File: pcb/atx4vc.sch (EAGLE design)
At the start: 76 parts, among them IC2 REG1117, IC3 STM32F042F4, IC4 MY_7905DT, J1 ATX24RH, SW1 324_SW, SW2 324_SW, SW3 324_SW, SW4 324_SW, SW5 324_SW, SW7 324_SW, U1 USBC_16P, U2 USBC_16P

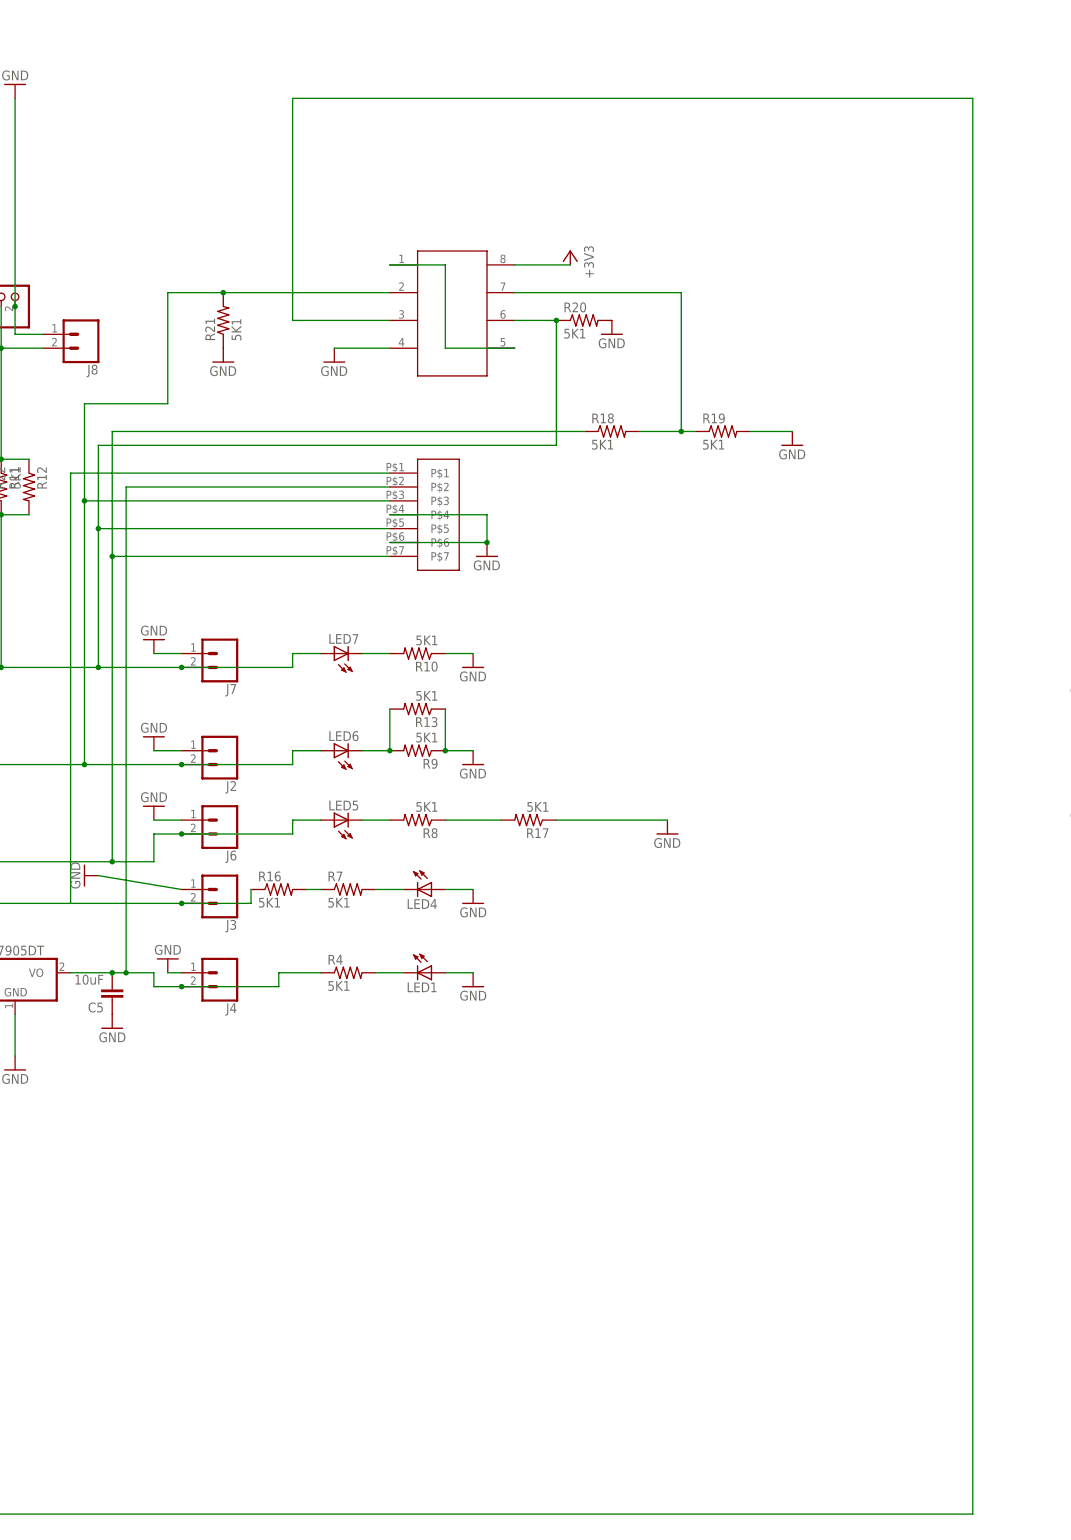
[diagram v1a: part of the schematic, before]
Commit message: updated fuse detect chip trace
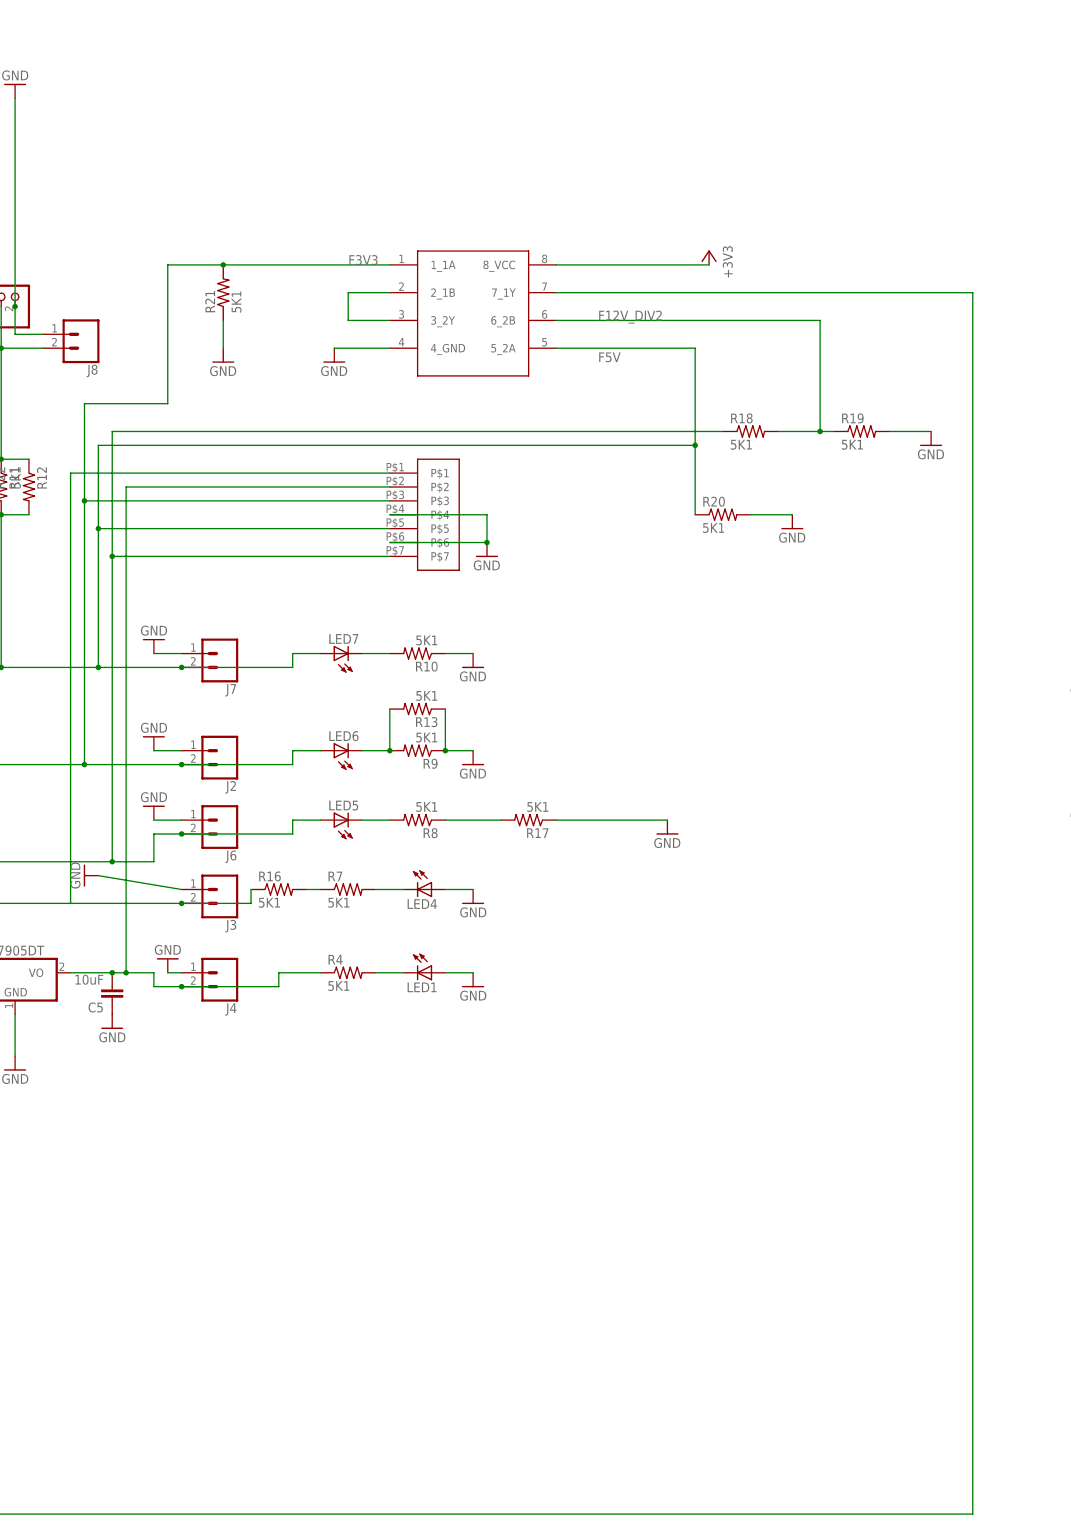
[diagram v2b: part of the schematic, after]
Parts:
- U$6: value 74LVC2G08SSOP8 -> 74LVC2G08; device atx4vc:74LVC2G08SSOP8 -> atx4vc:74LVC2G08
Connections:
- net N$15 renamed F12V
- removed net N$16: J2.2, LED6.A, R21.2, U$4.P$3, U$6.2_1B, U$7.B0, U$7.B1
- removed net N$30: J7.2, JP12.1, JP7.1, LED7.A, R11.2, R12.2, R20.1, R22.2, U$4.P$5, U$6.6_2B, U$8.B0, U$8.B1, U1.VBUS
- removed net N$39: R18.2, R19.1, U$6.7_1Y
- new net F12V_DIV2: R18.2, R19.1, U$6.6_2B
- new net F3V3: J2.2, LED6.A, R21.2, U$4.P$3, U$6.1_1A, U$7.B0, U$7.B1
- new net F5V: J7.2, JP12.1, JP7.1, LED7.A, R11.2, R12.2, R20.1, R22.2, U$4.P$5, U$6.5_2A, U$8.B0, U$8.B1, U1.VBUS
- net N$12: now also U$6.2_1B, U$6.3_2Y; no longer U$6.1_1A, U$6.5_2A
- net N$24: now also U$6.7_1Y; no longer U$6.3_2Y
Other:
- moved on the sheet: R18, R19, R20, R21
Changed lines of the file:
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@@
 <part name="JP13" library="SparkFun-Jumpers" deviceset="JUMPER-SMT_2_NO" device="_NO-SILK"/>
 <part name="JP14" library="SparkFun-Jumpers" deviceset="JUMPER-SMT_2_NO" device="_NO-SILK"/>
-<part name="U$6" library="atx4vc" deviceset="74LVC2G08" device="SSOP8"/>
+<part name="U$6" library="atx4vc" deviceset="74LVC2G08" device="" value="74LVC2G08"/>
 <part name="U$4" library="396_conn" deviceset="VH396" device=""/>
 <part name="JP10" library="adafruit" deviceset="PINHD-1X1" device="CB"/>
@@
 <attribute name="VALUE" x="401.32" y="58.42" size="1.778" layer="96"/>
 </instance>
-<instance part="+3V4" gate="G$1" x="419.1" y="116.84" smashed="yes" rot="MR0">
-<attribute name="VALUE" x="421.64" y="111.76" size="1.778" layer="96" rot="MR90"/>
+<instance part="+3V4" gate="G$1" x="444.5" y="116.84" smashed="yes" rot="MR0">
+<attribute name="VALUE" x="447.04" y="111.76" size="1.778" layer="96" rot="MR90"/>
 </instance>
 <instance part="GND38" gate="1" x="375.92" y="96.52" smashed="yes">
@@
 <attribute name="VALUE" x="-34.29" y="-119.38" size="1.778" layer="96"/>
 </instance>
-<instance part="R18" gate="G$1" x="426.72" y="83.82" smashed="yes">
-<attribute name="NAME" x="422.91" y="85.3186" size="1.778" layer="95"/>
-<attribute name="VALUE" x="422.91" y="80.518" size="1.778" layer="96"/>
-</instance>
-<instance part="R19" gate="G$1" x="447.04" y="83.82" smashed="yes">
-<attribute name="NAME" x="443.23" y="85.3186" size="1.778" layer="95"/>
-<attribute name="VALUE" x="443.23" y="80.518" size="1.778" layer="96"/>
-</instance>
-<instance part="GND39" gate="1" x="459.74" y="81.28" smashed="yes">
-<attribute name="VALUE" x="457.2" y="78.74" size="1.778" layer="96"/>
-</instance>
-<instance part="R20" gate="G$1" x="421.64" y="104.14" smashed="yes">
-<attribute name="NAME" x="417.83" y="105.6386" size="1.778" layer="95"/>
-<attribute name="VALUE" x="417.83" y="100.838" size="1.778" layer="96"/>
-</instance>
-<instance part="GND40" gate="1" x="426.72" y="101.6" smashed="yes">
-<attribute name="VALUE" x="424.18" y="99.06" size="1.778" layer="96"/>
-</instance>
-<instance part="R21" gate="G$1" x="355.6" y="104.14" smashed="yes" rot="R90">
-<attribute name="NAME" x="354.1014" y="100.33" size="1.778" layer="95" rot="R90"/>
-<attribute name="VALUE" x="358.902" y="100.33" size="1.778" layer="96" rot="R90"/>
+<instance part="R18" gate="G$1" x="452.12" y="83.82" smashed="yes">
+<attribute name="NAME" x="448.31" y="85.3186" size="1.778" layer="95"/>
+<attribute name="VALUE" x="448.31" y="80.518" size="1.778" layer="96"/>
+</instance>
+<instance part="R19" gate="G$1" x="472.44" y="83.82" smashed="yes">
+<attribute name="NAME" x="468.63" y="85.3186" size="1.778" layer="95"/>
+<attribute name="VALUE" x="468.63" y="80.518" size="1.778" layer="96"/>
+</instance>
+<instance part="GND39" gate="1" x="485.14" y="81.28" smashed="yes">
+<attribute name="VALUE" x="482.6" y="78.74" size="1.778" layer="96"/>
+</instance>
+<instance part="R20" gate="G$1" x="447.04" y="68.58" smashed="yes">
+<attribute name="NAME" x="443.23" y="70.0786" size="1.778" layer="95"/>
+<attribute name="VALUE" x="443.23" y="65.278" size="1.778" layer="96"/>
+</instance>
+<instance part="GND40" gate="1" x="459.74" y="66.04" smashed="yes">
+<attribute name="VALUE" x="457.2" y="63.5" size="1.778" layer="96"/>
+</instance>
+<instance part="R21" gate="G$1" x="355.6" y="109.22" smashed="yes" rot="R90">
+<attribute name="NAME" x="354.1014" y="105.41" size="1.778" layer="95" rot="R90"/>
+<attribute name="VALUE" x="358.902" y="105.41" size="1.778" layer="96" rot="R90"/>
 </instance>
 <instance part="GND41" gate="1" x="355.6" y="96.52" smashed="yes">
@@
 <pinref part="R19" gate="G$1" pin="2"/>
 <pinref part="GND39" gate="1" pin="GND"/>
-<wire x1="452.12" y1="83.82" x2="459.74" y2="83.82" width="0.1524" layer="91"/>
+<wire x1="477.52" y1="83.82" x2="485.14" y2="83.82" width="0.1524" layer="91"/>
 </segment>
 <segment>
 <pinref part="R20" gate="G$1" pin="2"/>
 <pinref part="GND40" gate="1" pin="GND"/>
+<wire x1="452.12" y1="68.58" x2="459.74" y2="68.58" width="0.1524" layer="91"/>
 </segment>
 <segment>
 <pinref part="R21" gate="G$1" pin="1"/>
 <pinref part="GND41" gate="1" pin="GND"/>
+<wire x1="355.6" y1="104.14" x2="355.6" y2="99.06" width="0.1524" layer="91"/>
 </segment>
 </net>
@@
 <pinref part="+3V4" gate="G$1" pin="+3V3"/>
 <pinref part="U$6" gate="G$1" pin="8_VCC"/>
-<wire x1="419.1" y1="114.3" x2="408.94" y2="114.3" width="0.1524" layer="91"/>
+<wire x1="444.5" y1="114.3" x2="416.56" y2="114.3" width="0.1524" layer="91"/>
 </segment>
 </net>
@@
 </segment>
 </net>
-<net name="N$30" class="0">
+<net name="F5V" class="0">
 <segment>
 <pinref part="LED7" gate="G$1" pin="A"/>
@@
 <junction x="332.74" y="40.64"/>
 <wire x1="332.74" y1="66.04" x2="332.74" y2="81.28" width="0.1524" layer="91"/>
-<wire x1="332.74" y1="81.28" x2="416.56" y2="81.28" width="0.1524" layer="91"/>
+<wire x1="332.74" y1="81.28" x2="441.96" y2="81.28" width="0.1524" layer="91"/>
 <junction x="332.74" y="66.04"/>
-<pinref part="U$6" gate="G$1" pin="6_2B"/>
-<wire x1="408.94" y1="104.14" x2="416.56" y2="104.14" width="0.1524" layer="91"/>
-<wire x1="416.56" y1="104.14" x2="416.56" y2="81.28" width="0.1524" layer="91"/>
+<wire x1="441.96" y1="68.58" x2="441.96" y2="81.28" width="0.1524" layer="91"/>
 <pinref part="R20" gate="G$1" pin="1"/>
-<junction x="416.56" y="104.14"/>
 <pinref part="R22" gate="G$1" pin="2"/>
 <wire x1="314.96" y1="68.58" x2="312.42" y2="68.58" width="0.1524" layer="91"/>
-</segment>
-</net>
-<net name="N$15" class="0">
+<pinref part="U$6" gate="G$1" pin="5_2A"/>
+<wire x1="441.96" y1="81.28" x2="441.96" y2="99.06" width="0.1524" layer="91"/>
+<wire x1="441.96" y1="99.06" x2="416.56" y2="99.06" width="0.1524" layer="91"/>
+<junction x="441.96" y="81.28"/>
+<label x="424.18" y="96.52" size="1.778" layer="95"/>
+</segment>
+</net>
+<net name="F12V" class="0">
 <segment>
 <pinref part="LED5" gate="G$1" pin="A"/>
@@
 <junction x="335.28" y="5.08"/>
 <wire x1="335.28" y1="60.96" x2="335.28" y2="83.82" width="0.1524" layer="91"/>
-<wire x1="335.28" y1="83.82" x2="421.64" y2="83.82" width="0.1524" layer="91"/>
+<wire x1="335.28" y1="83.82" x2="447.04" y2="83.82" width="0.1524" layer="91"/>
 <junction x="335.28" y="60.96"/>
 <pinref part="R18" gate="G$1" pin="1"/>
 </segment>
 </net>
-<net name="N$16" class="0">
+<net name="F3V3" class="0">
 <segment>
 <pinref part="LED6" gate="G$1" pin="A"/>
@@
 <junction x="330.2" y="71.12"/>
 <wire x1="330.2" y1="88.9" x2="345.44" y2="88.9" width="0.1524" layer="91"/>
-<wire x1="345.44" y1="88.9" x2="345.44" y2="109.22" width="0.1524" layer="91"/>
-<wire x1="345.44" y1="109.22" x2="355.6" y2="109.22" width="0.1524" layer="91"/>
-<pinref part="U$6" gate="G$1" pin="2_1B"/>
+<wire x1="345.44" y1="88.9" x2="345.44" y2="114.3" width="0.1524" layer="91"/>
+<wire x1="345.44" y1="114.3" x2="355.6" y2="114.3" width="0.1524" layer="91"/>
 <pinref part="R21" gate="G$1" pin="2"/>
-<wire x1="355.6" y1="109.22" x2="386.08" y2="109.22" width="0.1524" layer="91"/>
-<junction x="355.6" y="109.22"/>
+<pinref part="U$6" gate="G$1" pin="1_1A"/>
+<wire x1="355.6" y1="114.3" x2="386.08" y2="114.3" width="0.1524" layer="91"/>
+<junction x="355.6" y="114.3"/>
+<label x="378.46" y="114.3" size="1.778" layer="95"/>
 </segment>
 </net>
@@
 </segment>
 </net>
-<net name="N$12" class="0">
-<segment>
-<pinref part="U$6" gate="G$1" pin="5_2A"/>
-<wire x1="408.94" y1="99.06" x2="396.24" y2="99.06" width="0.1524" layer="91"/>
-<wire x1="396.24" y1="99.06" x2="396.24" y2="114.3" width="0.1524" layer="91"/>
-<pinref part="U$6" gate="G$1" pin="1_1A"/>
-<wire x1="396.24" y1="114.3" x2="386.08" y2="114.3" width="0.1524" layer="91"/>
-</segment>
-</net>
 <net name="N$24" class="0">
 <segment>
-<pinref part="U$6" gate="G$1" pin="3_2Y"/>
-<wire x1="386.08" y1="104.14" x2="368.3" y2="104.14" width="0.1524" layer="91"/>
-<wire x1="368.3" y1="104.14" x2="368.3" y2="144.78" width="0.1524" layer="91"/>
-<wire x1="368.3" y1="144.78" x2="492.76" y2="144.78" width="0.1524" layer="91"/>
-<wire x1="492.76" y1="144.78" x2="492.76" y2="-114.3" width="0.1524" layer="91"/>
+<wire x1="492.76" y1="109.22" x2="492.76" y2="-114.3" width="0.1524" layer="91"/>
 <wire x1="492.76" y1="-114.3" x2="-30.48" y2="-114.3" width="0.1524" layer="91"/>
 <pinref part="JP3" gate="G$1" pin="2"/>
+<pinref part="U$6" gate="G$1" pin="7_1Y"/>
+<wire x1="416.56" y1="109.22" x2="492.76" y2="109.22" width="0.1524" layer="91"/>
 </segment>
 </net>
@@
 </segment>
 </net>
-<net name="N$39" class="0">
+<net name="F12V_DIV2" class="0">
 <segment>
 <pinref part="R18" gate="G$1" pin="2"/>
 <pinref part="R19" gate="G$1" pin="1"/>
-<wire x1="441.96" y1="83.82" x2="439.42" y2="83.82" width="0.1524" layer="91"/>
-<pinref part="U$6" gate="G$1" pin="7_1Y"/>
-<wire x1="439.42" y1="83.82" x2="431.8" y2="83.82" width="0.1524" layer="91"/>
-<wire x1="439.42" y1="83.82" x2="439.42" y2="109.22" width="0.1524" layer="91"/>
-<wire x1="439.42" y1="109.22" x2="408.94" y2="109.22" width="0.1524" layer="91"/>
-<junction x="439.42" y="83.82"/>
-</segment>
-</net>
+<wire x1="467.36" y1="83.82" x2="464.82" y2="83.82" width="0.1524" layer="91"/>
+<wire x1="464.82" y1="83.82" x2="457.2" y2="83.82" width="0.1524" layer="91"/>
+<wire x1="464.82" y1="83.82" x2="464.82" y2="104.14" width="0.1524" layer="91"/>
+<junction x="464.82" y="83.82"/>
+<pinref part="U$6" gate="G$1" pin="6_2B"/>
+<wire x1="416.56" y1="104.14" x2="464.82" y2="104.14" width="0.1524" layer="91"/>
+<label x="424.18" y="104.14" size="1.778" layer="95"/>
+</segment>
+</net>
+<net name="N$12" class="0">
+<segment>
+<pinref part="U$6" gate="G$1" pin="3_2Y"/>
+<wire x1="386.08" y1="104.14" x2="378.46" y2="104.14" width="0.1524" layer="91"/>
+<wire x1="378.46" y1="104.14" x2="378.46" y2="109.22" width="0.1524" layer="91"/>
+<pinref part="U$6" gate="G$1" pin="2_1B"/>
+<wire x1="378.46" y1="109.22" x2="386.08" y2="109.22" width="0.1524" layer="91"/>
+</segment>
+</net>
